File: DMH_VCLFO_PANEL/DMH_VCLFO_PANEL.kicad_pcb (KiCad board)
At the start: 2 copper layers, 100 x 200 mm, 5 parts, among them J0 Panel_GND_Solder_Wire_Pad

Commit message: V1 one the panel ready
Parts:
- added H10: Sine, SynthStuff:Jack_6.35mm_Cutout_Output_v6, F.Cu at (124.8, 88.8)
- added H11: Random, SynthStuff:Jack_6.35mm_Cutout_Output_v6, F.Cu at (141.2, 88.8)
- added H12: Frequency, SynthStuff:Pot_Cutout_Medium_v2, F.Cu at (100.0, 60.8)
- added H13: CV Amt, SynthStuff:Pot_Cutout_Tiny_attv_P110KH1, F.Cu at (68.8, 60.8)
- added H14: LED A, SynthStuff:MountingHole_LED_3mm, F.Cu at (68.8, 78.0)
- added H15: LED A, SynthStuff:MountingHole_LED_3mm, F.Cu at (68.8, 138.0)
- added H16: Frequency, SynthStuff:Pot_Cutout_Medium_v2, F.Cu at (100.0, 120.8)
- added H17: Square, SynthStuff:Jack_6.35mm_Cutout_Output_v6, F.Cu at (75.2, 148.8)
- added H18: CV Amt, SynthStuff:Pot_Cutout_Tiny_attv_P110KH1, F.Cu at (68.8, 120.8)
- added H19: Triangle, SynthStuff:Jack_6.35mm_Cutout_Output_v6, F.Cu at (91.8, 148.8)
- added H20: CV, SynthStuff:Jack_6.35mm_Cutout_v3, F.Cu at (58.8, 148.8)
- added H21: Attenuvert, SynthStuff:Pot_Cutout_Tiny_attv_P110KH1, F.Cu at (131.2, 60.8)
- added H22: Ramp, SynthStuff:Jack_6.35mm_Cutout_Output_v6, F.Cu at (108.2, 148.8)
- added H23: Sine, SynthStuff:Jack_6.35mm_Cutout_Output_v6, F.Cu at (124.8, 148.8)
- added H24: Random, SynthStuff:Jack_6.35mm_Cutout_Output_v6, F.Cu at (141.2, 148.8)
- added H25: LED A, SynthStuff:MountingHole_LED_3mm, F.Cu at (68.8, 198.0)
- added H26: Frequency, SynthStuff:Pot_Cutout_Medium_v2, F.Cu at (100.0, 180.8)
- added H27: Square, SynthStuff:Jack_6.35mm_Cutout_Output_v6, F.Cu at (75.2, 208.8)
- added H28: CV Amt, SynthStuff:Pot_Cutout_Tiny_attv_P110KH1, F.Cu at (68.8, 180.8)
- added H29: Triangle, SynthStuff:Jack_6.35mm_Cutout_Output_v6, F.Cu at (91.8, 208.8)
- added H30: CV, SynthStuff:Jack_6.35mm_Cutout_v3, F.Cu at (58.8, 208.8)
- added H31: Attenuvert, SynthStuff:Pot_Cutout_Tiny_attv_P110KH1, F.Cu at (131.2, 120.8)
- added H32: Ramp, SynthStuff:Jack_6.35mm_Cutout_Output_v6, F.Cu at (108.2, 208.8)
- added H33: Sine, SynthStuff:Jack_6.35mm_Cutout_Output_v6, F.Cu at (124.8, 208.8)
- added H34: Random, SynthStuff:Jack_6.35mm_Cutout_Output_v6, F.Cu at (141.2, 208.8)
- added H35: Attenuvert, SynthStuff:Pot_Cutout_Tiny_attv_P110KH1, F.Cu at (131.2, 180.8)
- added H36: LED A, SynthStuff:MountingHole_LED_3mm, F.Cu at (131.2, 78.0)
- added H37: LED A, SynthStuff:MountingHole_LED_3mm, F.Cu at (131.2, 138.0)
- added H38: LED A, SynthStuff:MountingHole_LED_3mm, F.Cu at (131.2, 198.0)
- added H5: CV, SynthStuff:Jack_6.35mm_Cutout_v3, F.Cu at (58.8, 88.8)
- added H6: Square, SynthStuff:Jack_6.35mm_Cutout_Output_v6, F.Cu at (75.2, 88.8)
- added H7: Triangle, SynthStuff:Jack_6.35mm_Cutout_Output_v6, F.Cu at (91.8, 88.8)
- added H9: Ramp, SynthStuff:Jack_6.35mm_Cutout_Output_v6, F.Cu at (108.2, 88.8)
- moved J0 6.75 mm to (55.0, 136.8)
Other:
- board text added: "13700"
- board text added: "VCLFO"
- board text removed: "Name"
- board text removed: "TYPE"

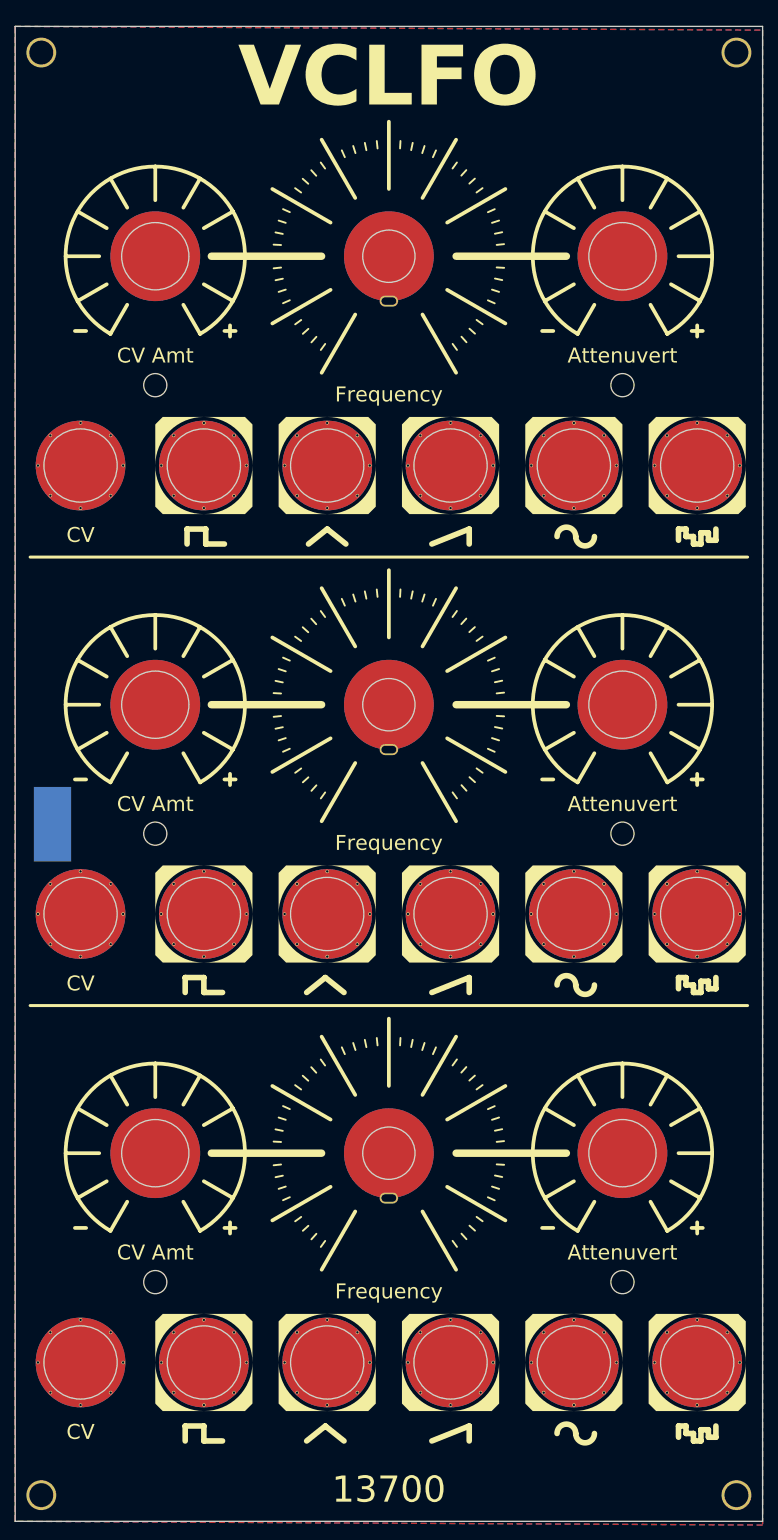
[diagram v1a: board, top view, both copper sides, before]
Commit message: V2 panel ready
- Removed attenuverter
- Re-added saw output
- Added sync input
- Added PLL switch
- Added unipolar switch
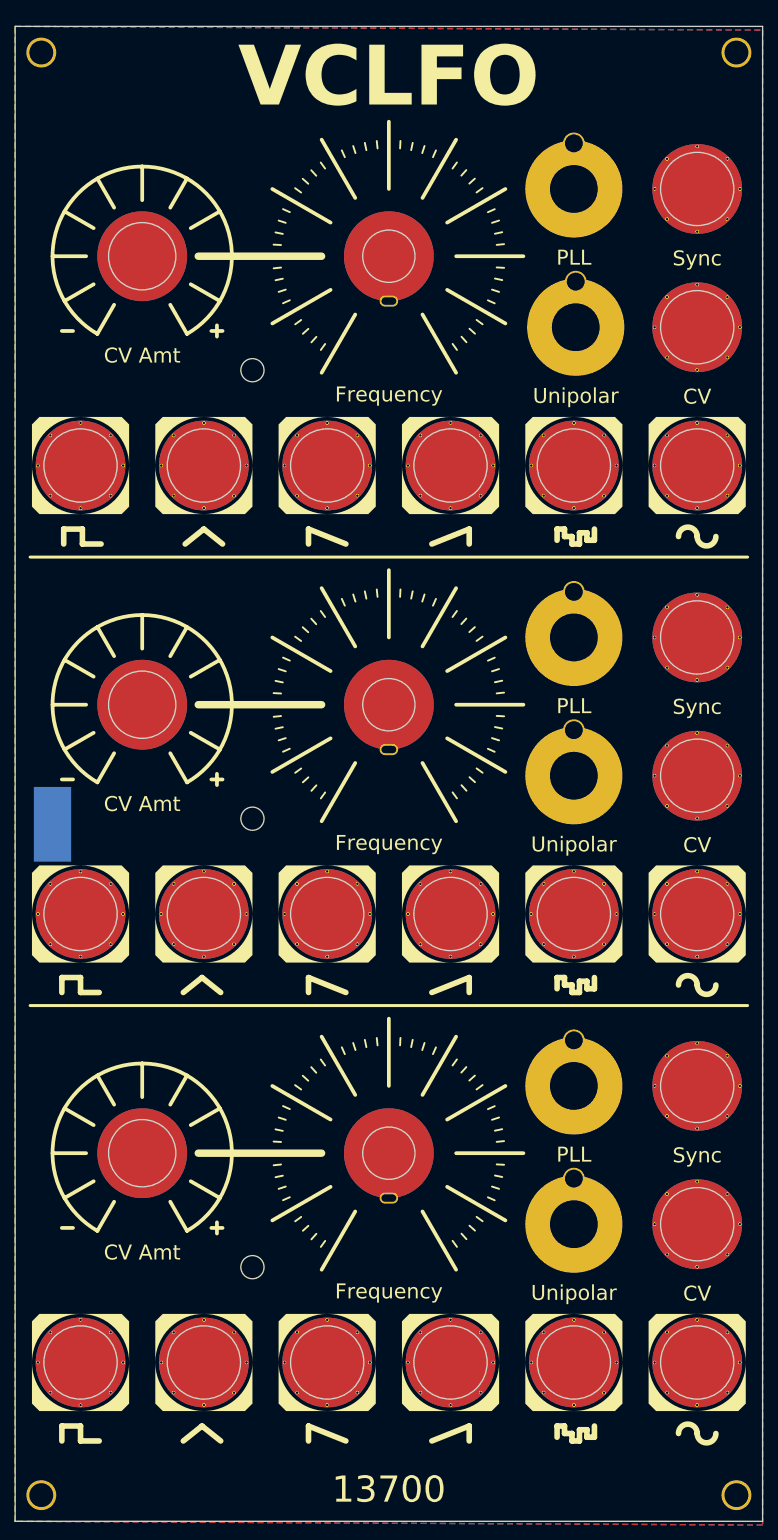
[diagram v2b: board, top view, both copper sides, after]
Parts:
- removed H36, H37, H38: LED A, SynthStuff:MountingHole_LED_3mm
- added H39: Saw, SynthStuff:Jack_6.35mm_Cutout_Output_v6, F.Cu at (91.8, 148.8)
- added H40: Saw, SynthStuff:Jack_6.35mm_Cutout_Output_v6, F.Cu at (91.8, 208.8)
- added H41: PLL, SynthStuff:Toggle_Switch_TE_Cutout, F.Cu at (124.8, 51.8)
- added H42: PLL, SynthStuff:Toggle_Switch_TE_Cutout, F.Cu at (124.8, 111.8)
- added H43: PLL, SynthStuff:Toggle_Switch_TE_Cutout, F.Cu at (124.8, 171.8)
- added H44: Unipolar, SynthStuff:Toggle_Switch_TE_Cutout, F.Cu at (125.0, 70.2)
- added H45: Unipolar, SynthStuff:Toggle_Switch_TE_Cutout, F.Cu at (124.8, 130.2)
- added H46: Unipolar, SynthStuff:Toggle_Switch_TE_Cutout, F.Cu at (124.8, 190.2)
- added H8: Saw, SynthStuff:Jack_6.35mm_Cutout_Output_v6, F.Cu at (91.8, 88.8)
- H21, H31, H35: value Attenuvert -> Sync; footprint SynthStuff:Pot_Cutout_Tiny_attv_P110KH1 -> SynthStuff:Jack_6.35mm_Cutout_v3
- moved H20 84.5 mm to (141.2, 130.2)
- moved H30 84.5 mm to (141.2, 190.2)
- moved H5 84.5 mm to (141.2, 70.2)
- moved H17 16.5 mm to (58.8, 148.8)
- moved H19 16.5 mm to (75.2, 148.8)
- moved H27 16.5 mm to (58.8, 208.8)
- moved H29 16.5 mm to (75.2, 208.8)
- moved H6 16.5 mm to (58.8, 88.8)
- moved H7 16.5 mm to (75.2, 88.8)
- moved H21 13.5 mm to (141.2, 51.8)
- moved H31 13.5 mm to (141.2, 111.8)
- moved H35 13.5 mm to (141.2, 171.8)
- moved H14 13.2 mm to (81.8, 76.0)
- moved H15 13.2 mm to (81.8, 136.0)
- moved H25 13.2 mm to (81.8, 196.0)
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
